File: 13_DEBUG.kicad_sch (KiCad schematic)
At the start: 0 parts

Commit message: updated schematics
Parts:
- added J1301: TC2030-CTX-NL_TARGET, symbol sportwatch_custom:TC2030_SWD
- added TP1301: VBAT, TestPoint:TestPoint_Pad_D1.0mm, symbol sportwatch_custom:TESTPAD
- added TP1302: VSYS, TestPoint:TestPoint_Pad_D1.0mm, symbol sportwatch_custom:TESTPAD
- added TP1303: VOUT1_1V8, TestPoint:TestPoint_Pad_D1.0mm, symbol sportwatch_custom:TESTPAD
- added TP1304: VOUT2_3V0_PROVISIONAL, TestPoint:TestPoint_Pad_D1.0mm, symbol sportwatch_custom:TESTPAD
- added TP1305: SYS_3V3, TestPoint:TestPoint_Pad_D1.0mm, symbol sportwatch_custom:TESTPAD
- added TP1306: GND, TestPoint:TestPoint_Pad_D1.0mm, symbol sportwatch_custom:TESTPAD
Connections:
- new net APOLLO_RST_N: J1301.3 (nRESET)
- new net APOLLO_SWCLK: J1301.4 (SWCLK)
- new net APOLLO_SWDIO: J1301.2 (SWDIO)
- new net APOLLO_SWO_GPIO28: J1301.6 (SWO)
- new net GND: J1301.5 (GND), TP1306.1 (TP)
- new net SYS_3V3: TP1305.1 (TP)
- new net VBAT: TP1301.1 (TP)
- new net VOUT1_1V8: J1301.1 (VTREF), TP1303.1 (TP)
- new net VOUT2_3V0_PROVISIONAL: TP1304.1 (TP)
- new net VSYS: TP1302.1 (TP)
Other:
- note added: "13_DEBUG — APOLLO510B SWD / SWO / RESET + REV-A POWER TEST PADS"
- note added: "All labels are still child-sheet-local. Final root integration must export VOUT1_1V8 / rails and connect APOLLO_SWDIO, APOLLO_SWCLK, APOLLO_RST_N, APOLLO_SWO_GPIO28 to 01_APOLLO510B."
- note added: "Apollo510B SWCLK is GPIO20 / ball M3 / function 0 SWDCK. SWDIO is GPIO21 / ball N3 / function 0 SWDIO. Reserve both from normal peripheral allocation."
- note added: "Apollo510B SWD supports up to 20 MHz, but the datasheet notes SWD read timing can require reduced SWCLK. Start bring-up around 4-10 MHz."
- note added: "External reset is dedicated ball H4 RSTN. Apollo includes an internal pull-up and reset debounce; no external pull-up or reset capacitor is added here."
- note added: "J1301 target pinout: 1=VTREF, 2=SWDIO, 3=nRESET, 4=SWCLK, 5=GND, 6=SWO. This matches the common TC2030 Cortex SWD mapping."
- note added: "Primary debug connector is a 6-pin TC2030 Cortex-SWD style target. No permanent header is required on the watch PCB."
- note added: "SWO is deliberately GPIO28 / ball L1 / function 0. The Ambiq Secure Bootloader already uses GPIO28 as a 1-Mbaud SWO boot-status output."
- note added: "SWO is optional for normal programming/debug. Apollo errata note SWO behavior in deep sleep and debugger reconnect corner cases; do not depend on SWO for production operation."
- note added: "TC2030 no-legs footprint and 1.0-mm test-pad footprints are intentionally subject to the dedicated pre-PCB footprint/mechanical audit."
- note added: "TP1301-TP1306 are Rev-A bring-up pads only. They provide quick access to battery/system rails before the enclosure is closed."
- note added: "VTREF is VOUT1_1V8 because GPIO20/21 belong to the VDDH I/O bank. The debugger should use this as target-voltage sense/reference, not as a board power source."
- title: (none) -> Rev-A — Apollo510B Debug / Bring-up

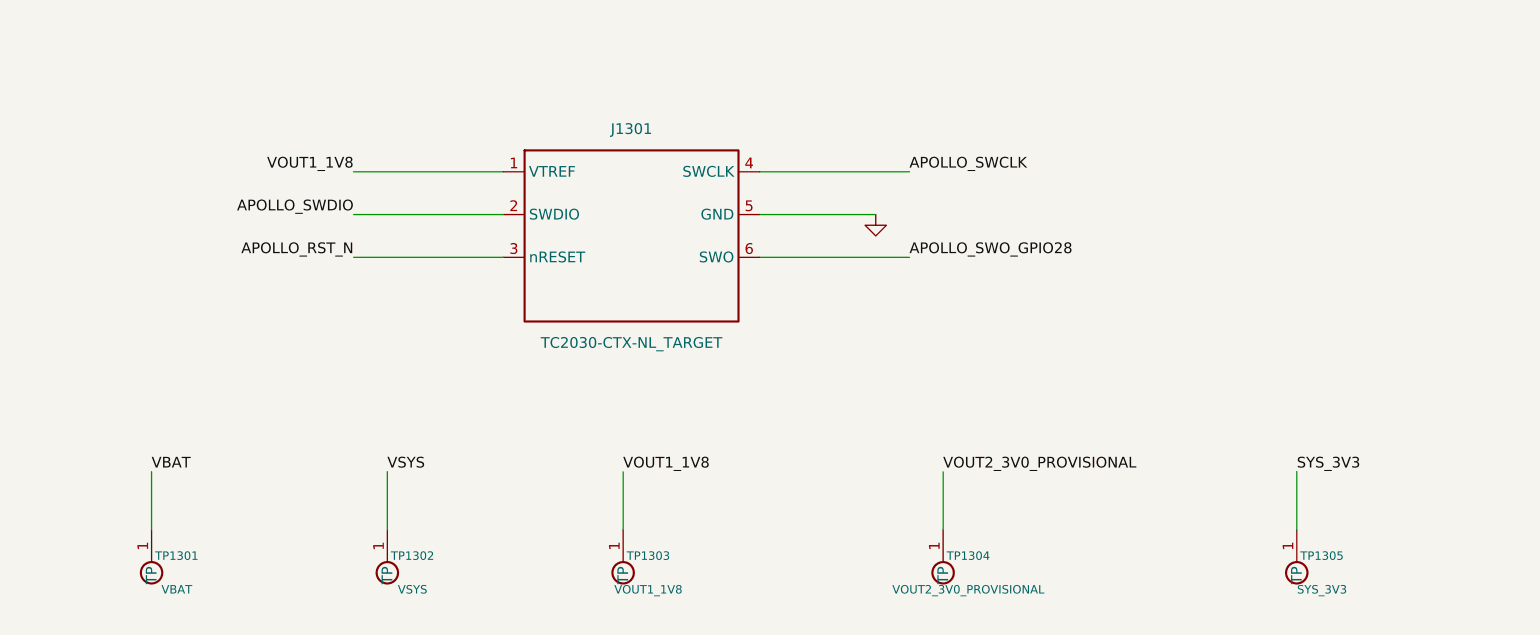
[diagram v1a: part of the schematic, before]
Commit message: refactor(kicad): integrate Rev-A hierarchy and libraries
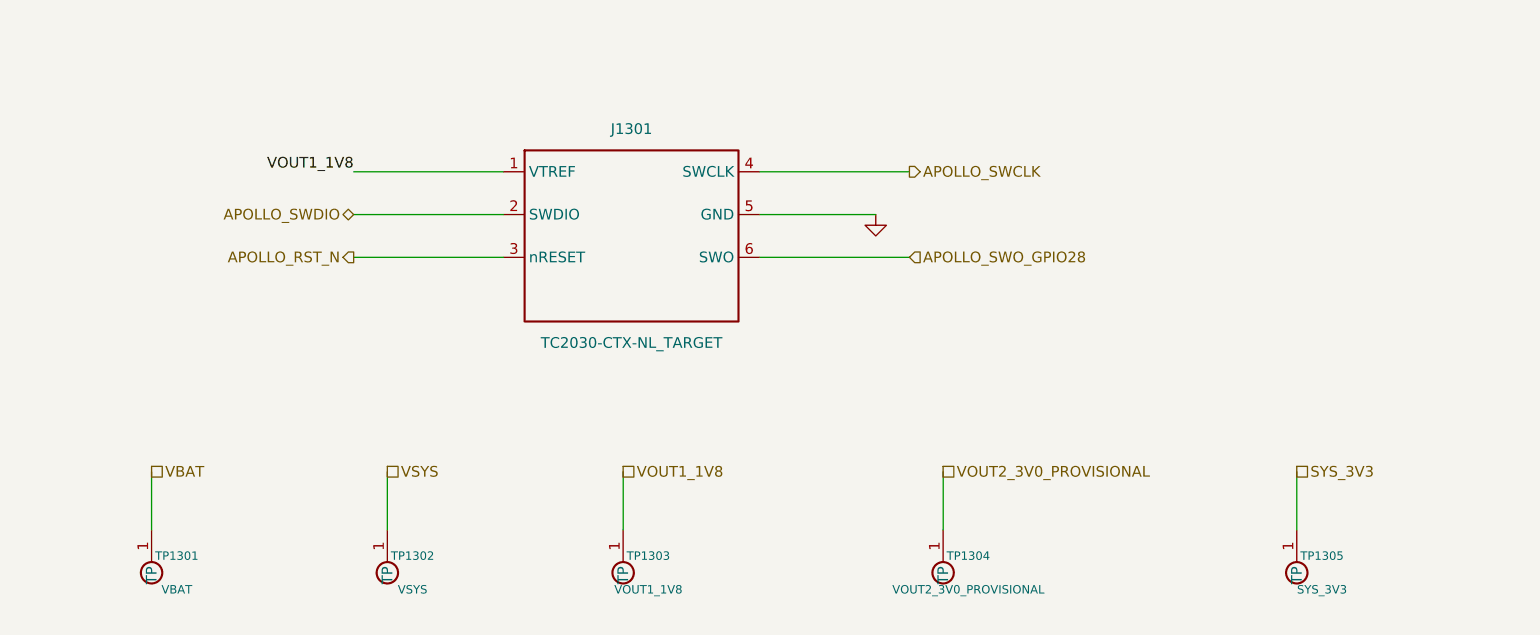
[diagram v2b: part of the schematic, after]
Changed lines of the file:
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@@
 		)
 	)
-	(label "VOUT1_1V8"
+	(hierarchical_label "VOUT1_1V8"
+		(shape passive)
 		(at 104 108 0)
 		(effects
@@
 		)
 	)
-	(label "VBAT"
+	(hierarchical_label "VBAT"
+		(shape passive)
 		(at 48 108 0)
 		(effects
@@
 		)
 	)
-	(label "SYS_3V3"
+	(hierarchical_label "SYS_3V3"
+		(shape passive)
 		(at 184 108 0)
 		(effects
@@
 		)
 	)
-	(label "APOLLO_RST_N"
+	(hierarchical_label "APOLLO_RST_N"
+		(shape output)
 		(at 72 82.54 180)
 		(effects
@@
 		)
 	)
-	(label "VSYS"
+	(hierarchical_label "VSYS"
+		(shape passive)
 		(at 76 108 0)
 		(effects
@@
 		)
 	)
-	(label "APOLLO_SWDIO"
+	(hierarchical_label "APOLLO_SWDIO"
+		(shape bidirectional)
 		(at 72 77.46 180)
 		(effects
@@
 		)
 	)
-	(label "VOUT2_3V0_PROVISIONAL"
+	(hierarchical_label "VOUT2_3V0_PROVISIONAL"
+		(shape passive)
 		(at 142 108 0)
 		(effects
@@
 		)
 	)
-	(label "APOLLO_SWO_GPIO28"
+	(hierarchical_label "APOLLO_SWO_GPIO28"
+		(shape input)
 		(at 138 82.54 0)
 		(effects
@@
 		)
 	)
-	(label "APOLLO_SWCLK"
+	(hierarchical_label "APOLLO_SWCLK"
+		(shape output)
 		(at 138 72.38 0)
 		(effects

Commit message: feat(kicad): assign and audit Rev-A footprints
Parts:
- J1301: footprint (none) -> Connector:Tag-Connect_TC2030-IDC-NL_2x03_P1.27mm_Vertical
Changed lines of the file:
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@@
 			)
 		)
-		(property "Footprint" ""
+		(property "Footprint" "Connector:Tag-Connect_TC2030-IDC-NL_2x03_P1.27mm_Vertical"
 			(at 105 80 0)
 			(hide yes)

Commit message: foundation correction
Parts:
- J1301, TP1301, TP1302, TP1303, TP1304, TP1305, TP1306: Board (none) -> MAIN
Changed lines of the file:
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@@
 			)
 		)
-	)
+(property "Board" "MAIN" (at 0 0 0) (effects (font (size 1 1)) (hide yes)))
+)
 	(symbol
 		(lib_id "sportwatch_custom:TESTPAD")
@@
 			)
 		)
-	)
+(property "Board" "MAIN" (at 0 0 0) (effects (font (size 1 1)) (hide yes)))
+)
 	(symbol
 		(lib_id "sportwatch_custom:TESTPAD")
@@
 			)
 		)
-	)
+(property "Board" "MAIN" (at 0 0 0) (effects (font (size 1 1)) (hide yes)))
+)
 	(symbol
 		(lib_id "power:GND")
@@
 			)
 		)
-	)
+(property "Board" "MAIN" (at 0 0 0) (effects (font (size 1 1)) (hide yes)))
+)
 	(symbol
 		(lib_id "sportwatch_custom:TC2030_SWD")
@@
 			)
 		)
-	)
+(property "Board" "MAIN" (at 0 0 0) (effects (font (size 1 1)) (hide yes)))
+)
 	(symbol
 		(lib_id "sportwatch_custom:TESTPAD")
@@
 			)
 		)
-	)
+(property "Board" "MAIN" (at 0 0 0) (effects (font (size 1 1)) (hide yes)))
+)
 	(symbol
 		(lib_id "sportwatch_custom:TESTPAD")
@@
 			)
 		)
-	)
+(property "Board" "MAIN" (at 0 0 0) (effects (font (size 1 1)) (hide yes)))
+)
 	(symbol
 		(lib_id "sportwatch_custom:TESTPAD")
@@
 			)
 		)
-	)
+(property "Board" "MAIN" (at 0 0 0) (effects (font (size 1 1)) (hide yes)))
+)
 	(symbol
 		(lib_id "sportwatch_custom:TESTPAD")
@@
 			)
 		)
-	)
-)
+(property "Board" "MAIN" (at 0 0 0) (effects (font (size 1 1)) (hide yes)))
+)
+)
